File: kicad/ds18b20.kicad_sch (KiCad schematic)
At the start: 4 parts

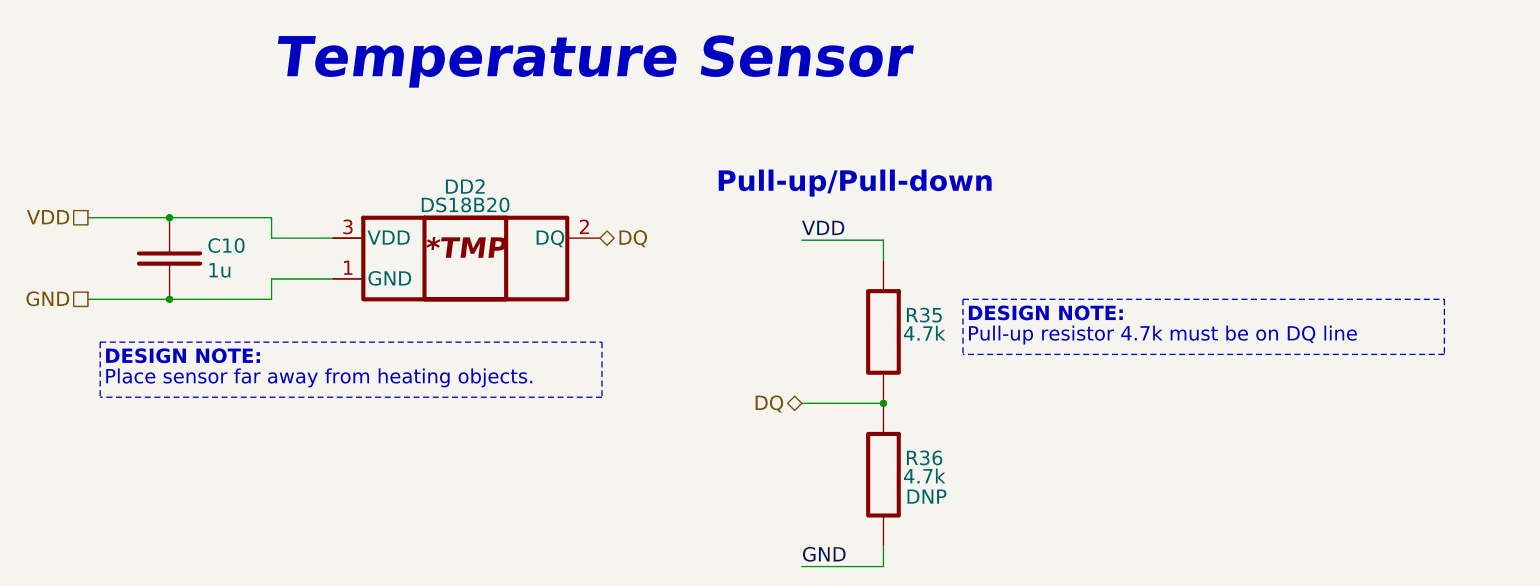
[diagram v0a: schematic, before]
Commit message: Reannotate schematic; Fix 5032 crystal footprint field; Update PCB with 5032 crystal
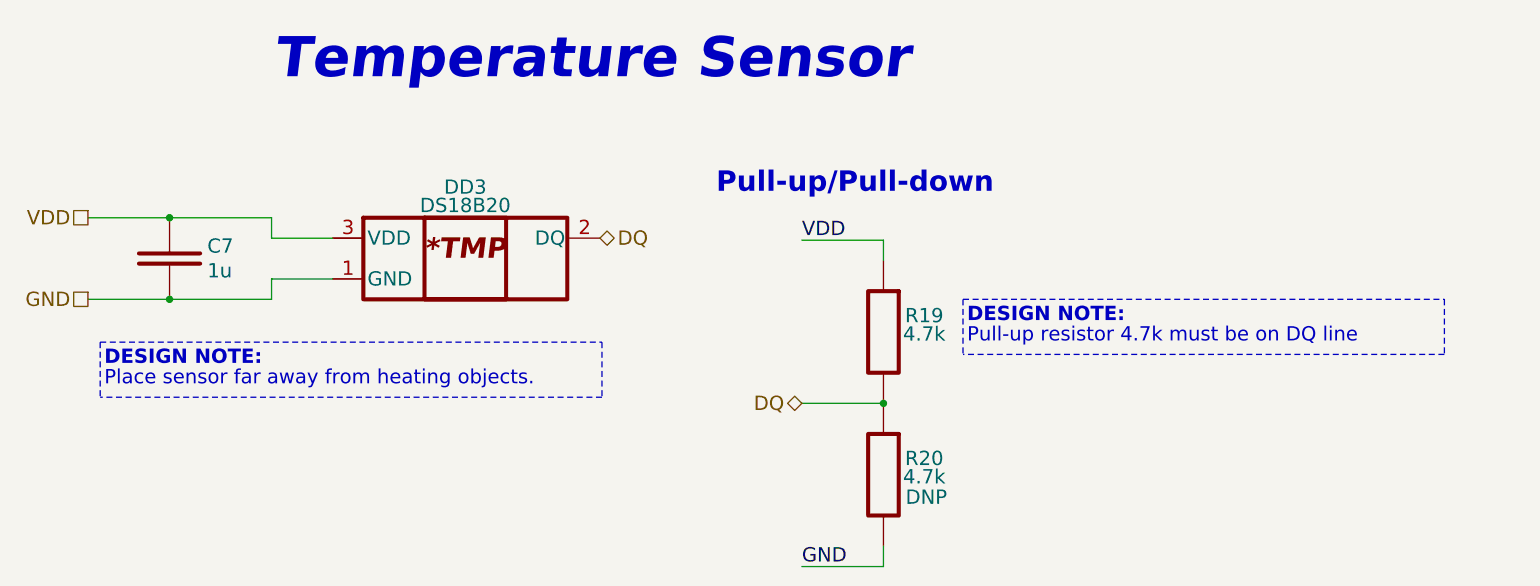
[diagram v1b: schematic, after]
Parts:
- renumbered C10 to C7, DD2 to DD3, R35 to R19, R36 to R20
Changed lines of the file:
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@@
   (symbol (lib_id "Capacitors:C_CAP") (at 100.584 79.756 270) (unit 1)
     (in_bom yes) (on_board yes)
-    (property "Reference" "C10" (id 0) (at 105.283 78.2066 90)
+    (property "Reference" "C7" (id 0) (at 105.283 78.2066 90)
       (effects (font (size 1.778 1.778)) (justify left))
     )
@@
   (symbol (lib_id "Resistors:R_RES") (at 189.484 106.68 270) (unit 1)
     (in_bom yes) (on_board yes)
-    (property "Reference" "R36" (id 0) (at 194.564 104.648 90)
+    (property "Reference" "R20" (id 0) (at 194.564 104.648 90)
       (effects (font (size 1.778 1.778)))
     )
@@
   (symbol (lib_id "Resistors:R_RES") (at 189.484 88.9 270) (unit 1)
     (in_bom yes) (on_board yes)
-    (property "Reference" "R35" (id 0) (at 194.564 86.868 90)
+    (property "Reference" "R19" (id 0) (at 194.564 86.868 90)
       (effects (font (size 1.778 1.778)))
     )
@@
   (symbol (lib_id "Chips:DS18B20") (at 137.414 74.676 0) (unit 1)
     (in_bom yes) (on_board yes)
-    (property "Reference" "DD2" (id 0) (at 137.414 70.866 0)
+    (property "Reference" "DD3" (id 0) (at 137.414 70.866 0)
       (effects (font (size 1.778 1.778)))
     )

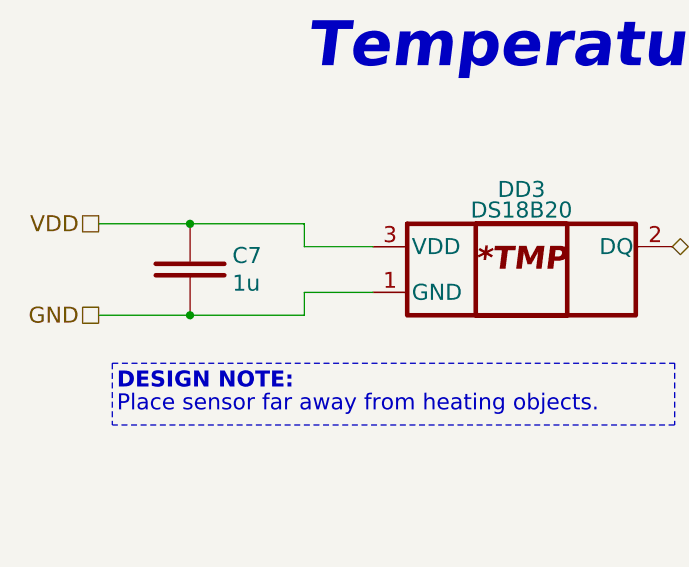
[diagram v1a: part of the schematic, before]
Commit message: Add voltage value to caps, update BOM, SCH, ASM
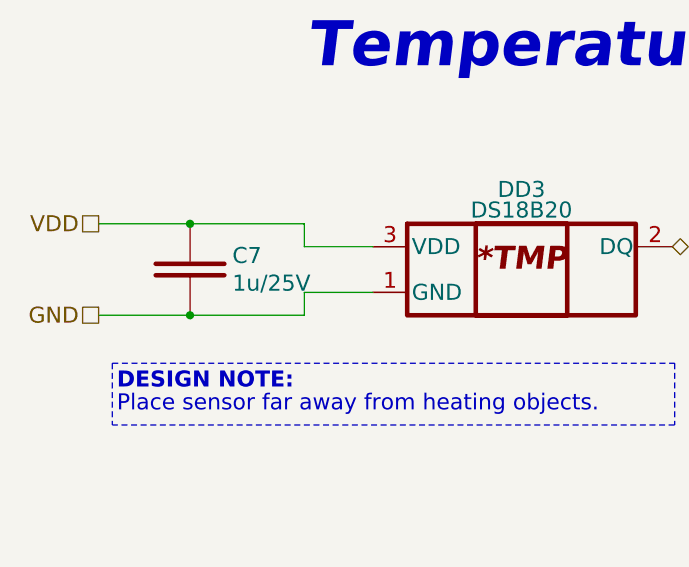
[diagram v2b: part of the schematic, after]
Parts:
- C7: value 1u -> 1u/25V; Case/Package (none) -> 0603; Tolerance (none) -> ±10%; Type (none) -> X7R
- R19, R20: Case/Package 0000 -> 0603; Tolerance ±% -> ±5%
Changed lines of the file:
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@@
       (effects (font (size 1.778 1.778)) (justify left))
     )
-    (property "Value" "1u" (id 1) (at 105.283 81.28 90)
+    (property "Value" "1u/25V" (id 1) (at 105.283 81.28 90)
       (effects (font (size 1.778 1.778)) (justify left))
     )
@@
       (effects (font (size 1.778 1.778)))
     )
+    (property "Voltage" "" (id 5) (at 100.584 79.756 0)
+      (effects (font (size 1.27 1.27)) hide)
+    )
+    (property "Case/Package" "0603" (id 6) (at 100.584 79.756 0)
+      (effects (font (size 1.27 1.27)) hide)
+    )
+    (property "Type" "X7R" (id 7) (at 90.424 79.756 0)
+      (effects (font (size 1.27 1.27)) hide)
+    )
+    (property "Tolerance" "±10%" (id 8) (at 87.884 79.756 0)
+      (effects (font (size 1.27 1.27)) hide)
+    )
     (pin "1")
     (pin "2")
   )
-  (symbol (lib_id "Resistors:R_RES") (at 189.484 106.68 270) (unit 1)
+  (symbol (lib_name "R_RES_1") (lib_id "Resistors:R_RES") (at 189.484 106.68 270) (unit 1)
     (in_bom yes) (on_board yes)
     (property "Reference" "R20" (id 0) (at 194.564 104.648 90)
@@
       (effects (font (size 1.778 1.778)))
     )
-    (property "Case/Package" "0000" (id 5) (at 183.134 106.68 0)
+    (property "Case/Package" "0603" (id 5) (at 183.134 106.68 0)
       (effects (font (size 1.27 1.27)) hide)
     )
@@
       (effects (font (size 1.27 1.27)) hide)
     )
-    (property "Tolerance" "±%" (id 7) (at 179.832 106.68 0)
+    (property "Tolerance" "±5%" (id 7) (at 179.832 106.68 0)
       (effects (font (size 1.27 1.27)) hide)
     )
+    (property "Part Number" "" (id 8) (at 189.484 106.68 0))
     (pin "1")
     (pin "2")
@@
       (effects (font (size 1.778 1.778)))
     )
-    (property "Case/Package" "0000" (id 5) (at 183.134 88.9 0)
+    (property "Case/Package" "0603" (id 5) (at 183.134 88.9 0)
       (effects (font (size 1.27 1.27)) hide)
     )
@@
       (effects (font (size 1.27 1.27)) hide)
     )
-    (property "Tolerance" "±%" (id 7) (at 179.832 88.9 0)
+    (property "Tolerance" "±5%" (id 7) (at 179.832 88.9 0)
       (effects (font (size 1.27 1.27)) hide)
     )
+    (property "Part Number" "" (id 8) (at 189.484 88.9 0))
     (pin "1")
     (pin "2")

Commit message: Add wiring diagram; Add work ours (stage 2); refactor folders
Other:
- title: (none) -> RadioSens v1
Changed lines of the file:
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@@
 (kicad_sch (version 20211123) (generator eeschema)
   (paper "A4")
+  (title_block
+    (title "RadioSens v1")
+    (comment 2 "Electrical Circuit")
+  )
   (junction (at 189.484 97.79) (diameter 0) (color 0 0 0 0)
   )
